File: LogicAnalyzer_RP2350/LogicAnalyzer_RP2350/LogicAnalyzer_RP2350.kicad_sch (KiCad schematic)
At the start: 0 parts

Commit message: Added USB VBUS Protection and component Libraries
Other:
- added sheet USB & POWER (USB & POWER.kicad_sch)
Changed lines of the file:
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@@
 	(generator_version "10.0")
 	(paper "A4")
+	(sheet
+		(at 31.75 30.48)
+		(size 34.29 36.83)
+		(exclude_from_sim no)
+		(in_bom yes)
+		(on_board yes)
+		(dnp no)
+		(fields_autoplaced yes)
+		(stroke
+			(width 0.1524)
+			(type solid)
+			(color 0 60 255 1)
+		)
+		(fill
+			(color 241 210 16 1)
+		)
+		(property "Sheetname" "USB & POWER"
+			(at 31.75 29.7684 0)
+			(show_name no)
+			(do_not_autoplace no)
+			(effects
+				(font
+					(size 1.27 1.27)
+				)
+				(justify left bottom)
+			)
+		)
+		(property "Sheetfile" "USB & POWER.kicad_sch"
+			(at 31.75 67.8946 0)
+			(show_name no)
+			(do_not_autoplace no)
+			(effects
+				(font
+					(size 1.27 1.27)
+				)
+				(justify left top)
+			)
+		)
+		(instances
+			(project "LogicAnalyzer_RP2350"
+				(path "/d75f24d0-99d8-459e-8e7b-473191ec3959"
+					(page "2")
+				)
+			)
+		)
+	)
 	(sheet_instances
 		(path "/"

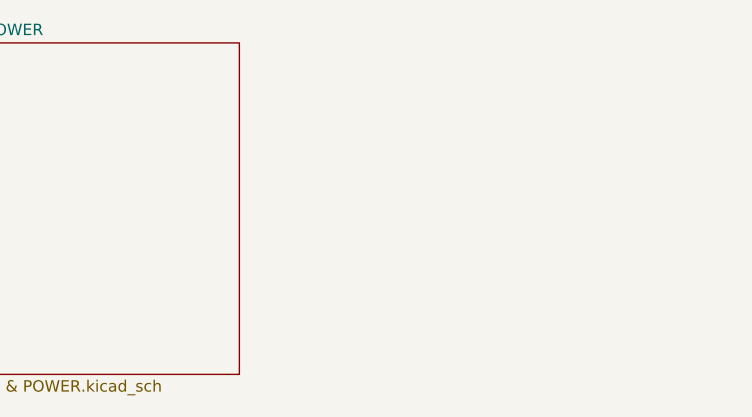
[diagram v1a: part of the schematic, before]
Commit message: added RP2350 Child Sheets and H Nets for USB
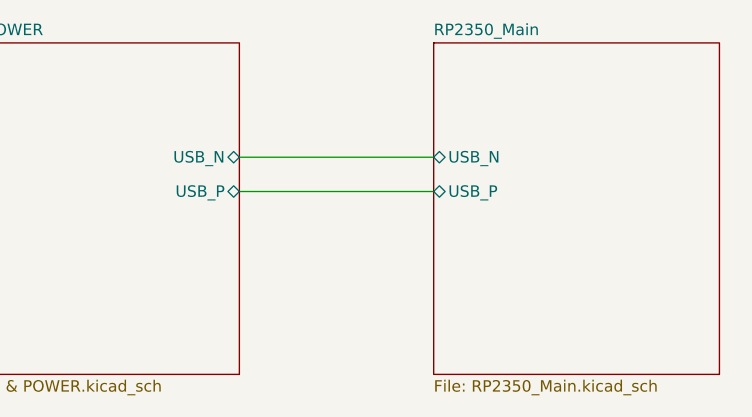
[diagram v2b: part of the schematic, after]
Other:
- added sheet RP2350_Main (RP2350_Main.kicad_sch)
- sheet USB & POWER ports: added USB_N, USB_P; removed none
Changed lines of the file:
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@@
 	(generator_version "10.0")
 	(paper "A4")
+	(wire
+		(pts
+			(xy 66.04 46.99) (xy 87.63 46.99)
+		)
+		(stroke
+			(width 0)
+			(type default)
+		)
+	)
+	(wire
+		(pts
+			(xy 66.04 43.18) (xy 87.63 43.18)
+		)
+		(stroke
+			(width 0)
+			(type default)
+		)
+	)
+	(sheet
+		(at 87.63 30.48)
+		(size 31.75 36.83)
+		(exclude_from_sim no)
+		(in_bom yes)
+		(on_board yes)
+		(dnp no)
+		(fields_autoplaced yes)
+		(stroke
+			(width 0.1524)
+			(type solid)
+			(color 0 0 0 1)
+		)
+		(fill
+			(color 255 255 194 1)
+		)
+		(property "Sheetname" "RP2350_Main"
+			(at 87.63 29.7684 0)
+			(show_name no)
+			(do_not_autoplace no)
+			(effects
+				(font
+					(size 1.27 1.27)
+				)
+				(justify left bottom)
+			)
+		)
+		(property "Sheetfile" "RP2350_Main.kicad_sch"
+			(at 87.63 67.8946 0)
+			(show_name no)
+			(do_not_autoplace no)
+			(effects
+				(font
+					(size 1.27 1.27)
+				)
+				(justify left top)
+			)
+		)
+		(pin "USB_N" bidirectional
+			(at 87.63 43.18 180)
+			(effects
+				(font
+					(size 1.27 1.27)
+				)
+				(justify left)
+			)
+		)
+		(pin "USB_P" bidirectional
+			(at 87.63 46.99 180)
+			(effects
+				(font
+					(size 1.27 1.27)
+				)
+				(justify left)
+			)
+		)
+		(instances
+			(project "LogicAnalyzer_RP2350"
+				(path "/d75f24d0-99d8-459e-8e7b-473191ec3959"
+					(page "3")
+				)
+			)
+		)
+	)
 	(sheet
 		(at 31.75 30.48)
@@
 			(width 0.1524)
 			(type solid)
-			(color 0 60 255 1)
+			(color 0 0 0 1)
 		)
 		(fill
-			(color 241 210 16 1)
+			(color 255 255 194 1)
 		)
 		(property "Sheetname" "USB & POWER"
@@
 			)
 		)
+		(pin "USB_N" bidirectional
+			(at 66.04 43.18 0)
+			(effects
+				(font
+					(size 1.27 1.27)
+				)
+				(justify right)
+			)
+		)
+		(pin "USB_P" bidirectional
+			(at 66.04 46.99 0)
+			(effects
+				(font
+					(size 1.27 1.27)
+				)
+				(justify right)
+			)
+		)

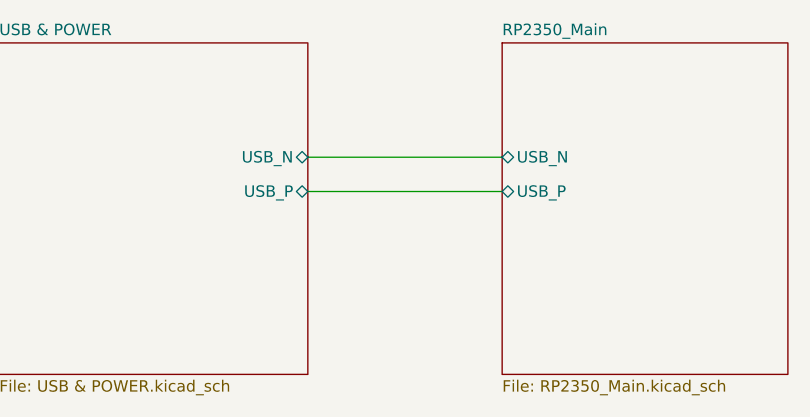
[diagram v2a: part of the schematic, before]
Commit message: QSPIFLASH ADDED
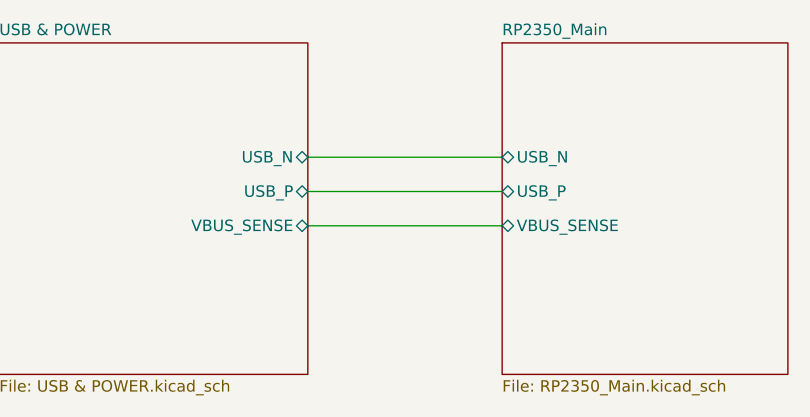
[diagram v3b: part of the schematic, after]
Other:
- sheet RP2350_Main ports: added VBUS_SENSE; removed none
- sheet USB & POWER ports: added VBUS_SENSE; removed none
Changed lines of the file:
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@@
+		)
+	)
+	(wire
+		(pts
+			(xy 66.04 50.8) (xy 87.63 50.8)
+		)
+		(stroke
+			(width 0)
+			(type default)
 		)
 	)
@@
 		(pin "USB_P" bidirectional
 			(at 87.63 46.99 180)
+			(effects
+				(font
+					(size 1.27 1.27)
+				)
+				(justify left)
+			)
+		)
+		(pin "VBUS_SENSE" bidirectional
+			(at 87.63 50.8 180)
 			(effects
 				(font
@@
 			(effects
 				(font
+					(size 1.27 1.27)
+				)
+				(justify right)
+			)
+		)
+		(pin "VBUS_SENSE" bidirectional
+			(at 66.04 50.8 0)
+			(effects
+				(font

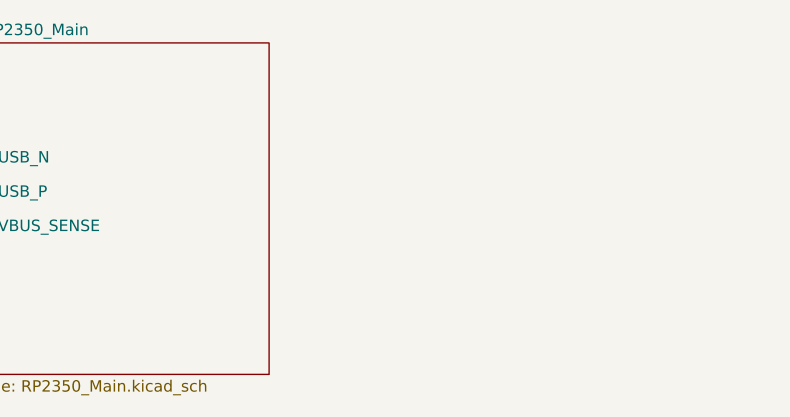
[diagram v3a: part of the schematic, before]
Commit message: Added Buses for Logic Input Pins and Sheet for Shift Registers
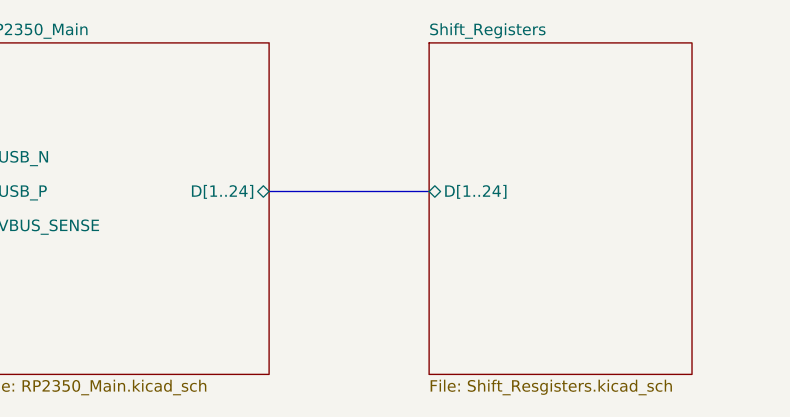
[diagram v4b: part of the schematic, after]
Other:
- added sheet Shift_Registers (Shift_Resgisters.kicad_sch)
- sheet RP2350_Main ports: added D[1..24]; removed none
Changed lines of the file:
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@@
+		)
+	)
+	(bus
+		(pts
+			(xy 119.38 46.99) (xy 137.16 46.99)
+		)
+		(stroke
+			(width 0)
+			(type default)
 		)
 	)
@@
 			)
 		)
+		(pin "D[1..24]" bidirectional
+			(at 119.38 46.99 0)
+			(effects
+				(font
+					(size 1.27 1.27)
+				)
+				(justify right)
+			)
+		)
 		(instances
 			(project "LogicAnalyzer_RP2350"
@@
 				)
 			)
+		)
+	)
+	(sheet
+		(at 137.16 30.48)
+		(size 29.21 36.83)
+		(exclude_from_sim no)
+		(in_bom yes)
+		(on_board yes)
+		(dnp no)
+		(fields_autoplaced yes)
+		(stroke
+			(width 0.1524)
+			(type solid)
+		)
+		(fill
+			(color 255 255 194 1)
+		)
+		(property "Sheetname" "Shift_Registers"
+			(at 137.16 29.7684 0)
+			(show_name no)
+			(do_not_autoplace no)
+			(effects
+				(font
+					(size 1.27 1.27)
+				)
+				(justify left bottom)
+			)
+		)
+		(property "Sheetfile" "Shift_Resgisters.kicad_sch"
+			(at 137.16 67.8946 0)
+			(show_name no)
+			(do_not_autoplace no)
+			(effects
+				(font
+					(size 1.27 1.27)
+				)
+				(justify left top)
+			)
+		)
+		(pin "D[1..24]" bidirectional
+			(at 137.16 46.99 180)
+			(effects
+				(font
+					(size 1.27 1.27)
+				)
+				(justify left)
+			)
+		)
+		(instances
+			(project "LogicAnalyzer_RP2350"
+				(path "/d75f24d0-99d8-459e-8e7b-473191ec3959"
+					(page "4")
+				)
+			)

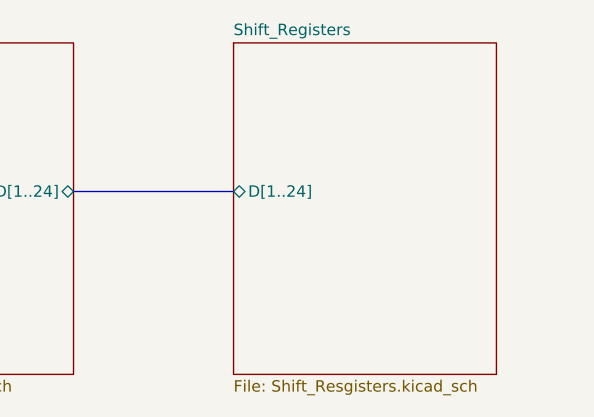
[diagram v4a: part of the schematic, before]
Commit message: Added Level Shifter TXU Series
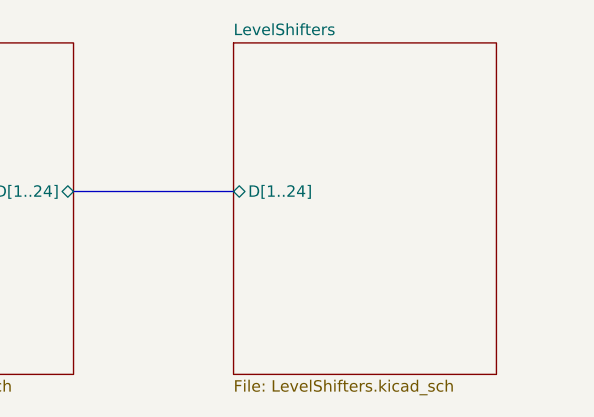
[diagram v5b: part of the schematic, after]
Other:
- sheet Shift_Registers renamed LevelShifters
- sheet LevelShifters: file Shift_Resgisters.kicad_sch -> LevelShifters.kicad_sch
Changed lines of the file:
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@@
 			(color 255 255 194 1)
 		)
-		(property "Sheetname" "Shift_Registers"
+		(property "Sheetname" "LevelShifters"
 			(at 137.16 29.7684 0)
 			(show_name no)
@@
 			)
 		)
-		(property "Sheetfile" "Shift_Resgisters.kicad_sch"
+		(property "Sheetfile" "LevelShifters.kicad_sch"
 			(at 137.16 67.8946 0)
 			(show_name no)

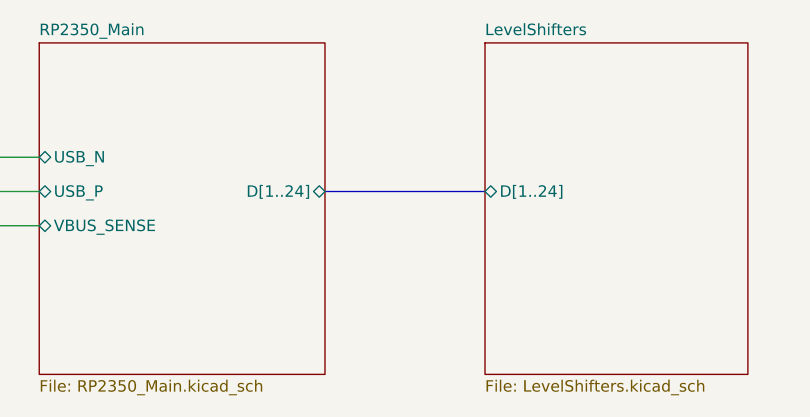
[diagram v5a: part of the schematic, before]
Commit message: Added EXT VREF, TRIG, ROTARY SWITCH, DAISY CHAIN CONNECTIONS etc
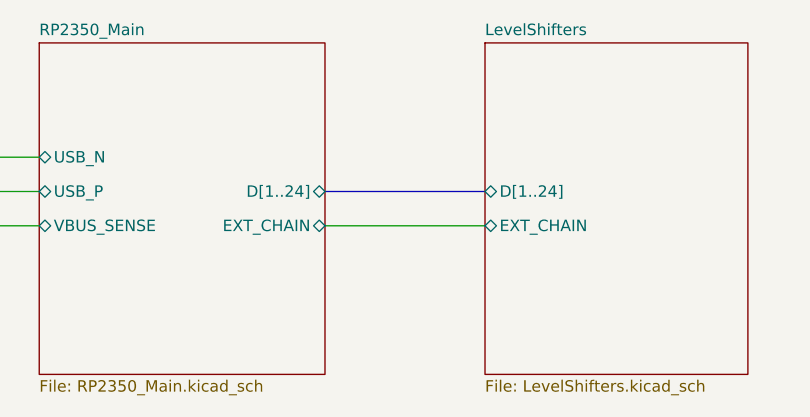
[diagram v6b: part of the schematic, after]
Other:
- sheet LevelShifters ports: added EXT_CHAIN; removed none
- sheet RP2350_Main ports: added EXT_CHAIN; removed none
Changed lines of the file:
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@@
+		)
+	)
+	(wire
+		(pts
+			(xy 119.38 50.8) (xy 137.16 50.8)
+		)
+		(stroke
+			(width 0)
+			(type default)
 		)
 	)
@@
 			)
 		)
+		(pin "EXT_CHAIN" bidirectional
+			(at 119.38 50.8 0)
+			(effects
+				(font
+					(size 1.27 1.27)
+				)
+				(justify right)
+			)
+		)
 		(instances
 			(project "LogicAnalyzer_RP2350"
@@
 			(effects
 				(font
+					(size 1.27 1.27)
+				)
+				(justify left)
+			)
+		)
+		(pin "EXT_CHAIN" bidirectional
+			(at 137.16 50.8 180)
+			(effects
+				(font

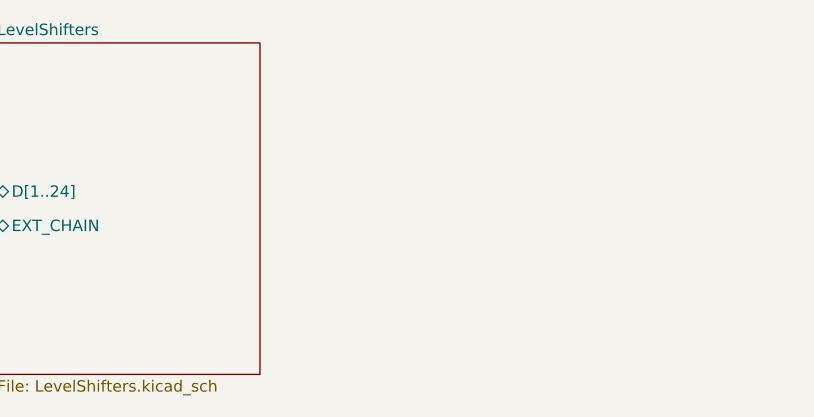
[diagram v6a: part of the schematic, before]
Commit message: Connector for Front Panel Interface Added
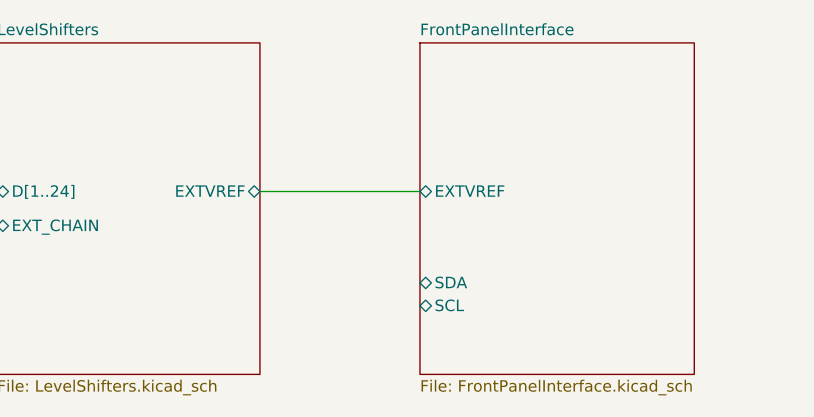
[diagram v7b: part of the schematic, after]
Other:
- added sheet FrontPanelInterface (FrontPanelInterface.kicad_sch)
- sheet LevelShifters ports: added EXTVREF; removed none
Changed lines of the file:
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@@
+	(wire
+		(pts
+			(xy 166.37 46.99) (xy 184.15 46.99)
+		)
+		(stroke
+			(width 0)
+			(type default)
+		)
+	)
 	(wire
 		(pts
@@
 	)
 	(sheet
+		(at 184.15 30.48)
+		(size 30.48 36.83)
+		(exclude_from_sim no)
+		(in_bom yes)
+		(on_board yes)
+		(dnp no)
+		(fields_autoplaced yes)
+		(stroke
+			(width 0.1524)
+			(type solid)
+		)
+		(fill
+			(color 255 255 194 1)
+		)
+		(property "Sheetname" "FrontPanelInterface"
+			(at 184.15 29.7684 0)
+			(show_name no)
+			(do_not_autoplace no)
+			(effects
+				(font
+					(size 1.27 1.27)
+				)
+				(justify left bottom)
+			)
+		)
+		(property "Sheetfile" "FrontPanelInterface.kicad_sch"
+			(at 184.15 67.8946 0)
+			(show_name no)
+			(do_not_autoplace no)
+			(effects
+				(font
+					(size 1.27 1.27)
+				)
+				(justify left top)
+			)
+		)
+		(pin "EXTVREF" bidirectional
+			(at 184.15 46.99 180)
+			(effects
+				(font
+					(size 1.27 1.27)
+				)
+				(justify left)
+			)
+		)
+		(pin "SDA" bidirectional
+			(at 184.15 57.15 180)
+			(effects
+				(font
+					(size 1.27 1.27)
+				)
+				(justify left)
+			)
+		)
+		(pin "SCL" bidirectional
+			(at 184.15 59.69 180)
+			(effects
+				(font
+					(size 1.27 1.27)
+				)
+				(justify left)
+			)
+		)
+		(instances
+			(project "LogicAnalyzer_RP2350"
+				(path "/d75f24d0-99d8-459e-8e7b-473191ec3959"
+					(page "5")
+				)
+			)
+		)
+	)
+	(sheet
 		(at 31.75 30.48)
 		(size 34.29 36.83)
@@
 			)
 		)
+		(pin "EXTVREF" bidirectional
+			(at 166.37 46.99 0)
+			(effects
+				(font
+					(size 1.27 1.27)
+				)
+				(justify right)
+			)
+		)
